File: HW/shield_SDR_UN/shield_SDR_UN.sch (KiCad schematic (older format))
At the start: 1 part

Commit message: Subsystems sheets created
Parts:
- removed U?: XC6SLX9-TQG144, symbol FPGA_Xilinx_Spartan6:XC6SLX9-TQG144
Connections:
- wire segments 2 -> 0
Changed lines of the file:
@@
 $Descr A3 16535 11693
 encoding utf-8
-Sheet 1 1
+Sheet 1 5
 Title ""
 Date ""
@@
 Comment4 ""
 $EndDescr
-$Comp
-L FPGA_Xilinx_Spartan6:XC6SLX9-TQG144 U?
-U 1 1 5CC13A59
-P 4200 3250
-F 0 "U?" H 4200 1475 50  0000 C CNN
-F 1 "XC6SLX9-TQG144" H 4200 1384 50  0000 C CNN
-F 2 "" H 4200 3250 50  0001 C CNN
-F 3 "" H 4200 3250 50  0000 C CNN
-	1    4200 3250
-	1    0    0    -1
-$EndComp
-Wire Wire Line
-	2600 1550 2700 1550
-Wire Wire Line
-	2700 1550 2800 1550
-Connection ~ 2700 1550
+$Sheet
+S 3900 2800 1100 300
+U 5CC081D2
+F0 "rf_front_end" 50
+F1 "rf_front_end.sch" 50
+$EndSheet
+$Sheet
+S 3900 3350 1100 300
+U 5CC08265
+F0 "FPGA" 50
+F1 "FPGA.sch" 50
+$EndSheet
+$Sheet
+S 3900 3900 1100 300
+U 5CC082AD
+F0 "proc" 50
+F1 "proc.sch" 50
+$EndSheet
+$Sheet
+S 3900 4500 1100 300
+U 5CC08321
+F0 "power" 50
+F1 "power.sch" 50
+$EndSheet
 $EndSCHEMATC

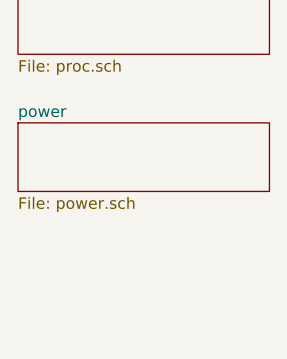
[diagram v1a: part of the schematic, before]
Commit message: Onion 2 routed
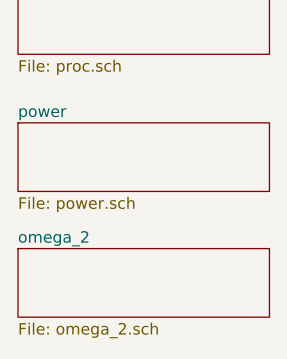
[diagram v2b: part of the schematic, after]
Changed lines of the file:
@@
 $Descr A3 16535 11693
 encoding utf-8
-Sheet 1 5
+Sheet 1 6
 Title ""
 Date ""
@@
 F1 "power.sch" 50
 $EndSheet
+$Sheet
+S 3900 5050 1100 300
+U 5CFB52DC
+F0 "omega_2" 50
+F1 "omega_2.sch" 50
+$EndSheet
 $EndSCHEMATC

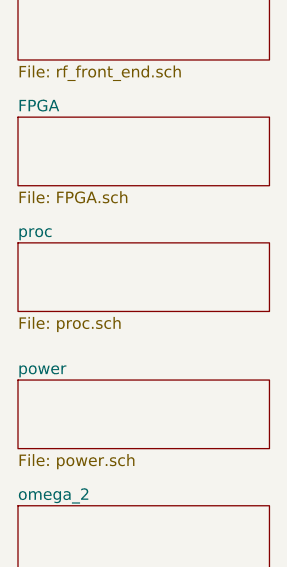
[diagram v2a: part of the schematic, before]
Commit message: se agrego el chip multirelojes
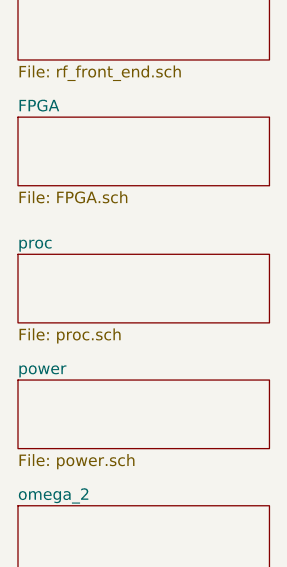
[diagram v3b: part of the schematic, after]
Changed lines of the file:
@@
 $EndSheet
 $Sheet
-S 3900 3900 1100 300
+S 3900 3950 1100 300
 U 5CC082AD
 F0 "proc" 50

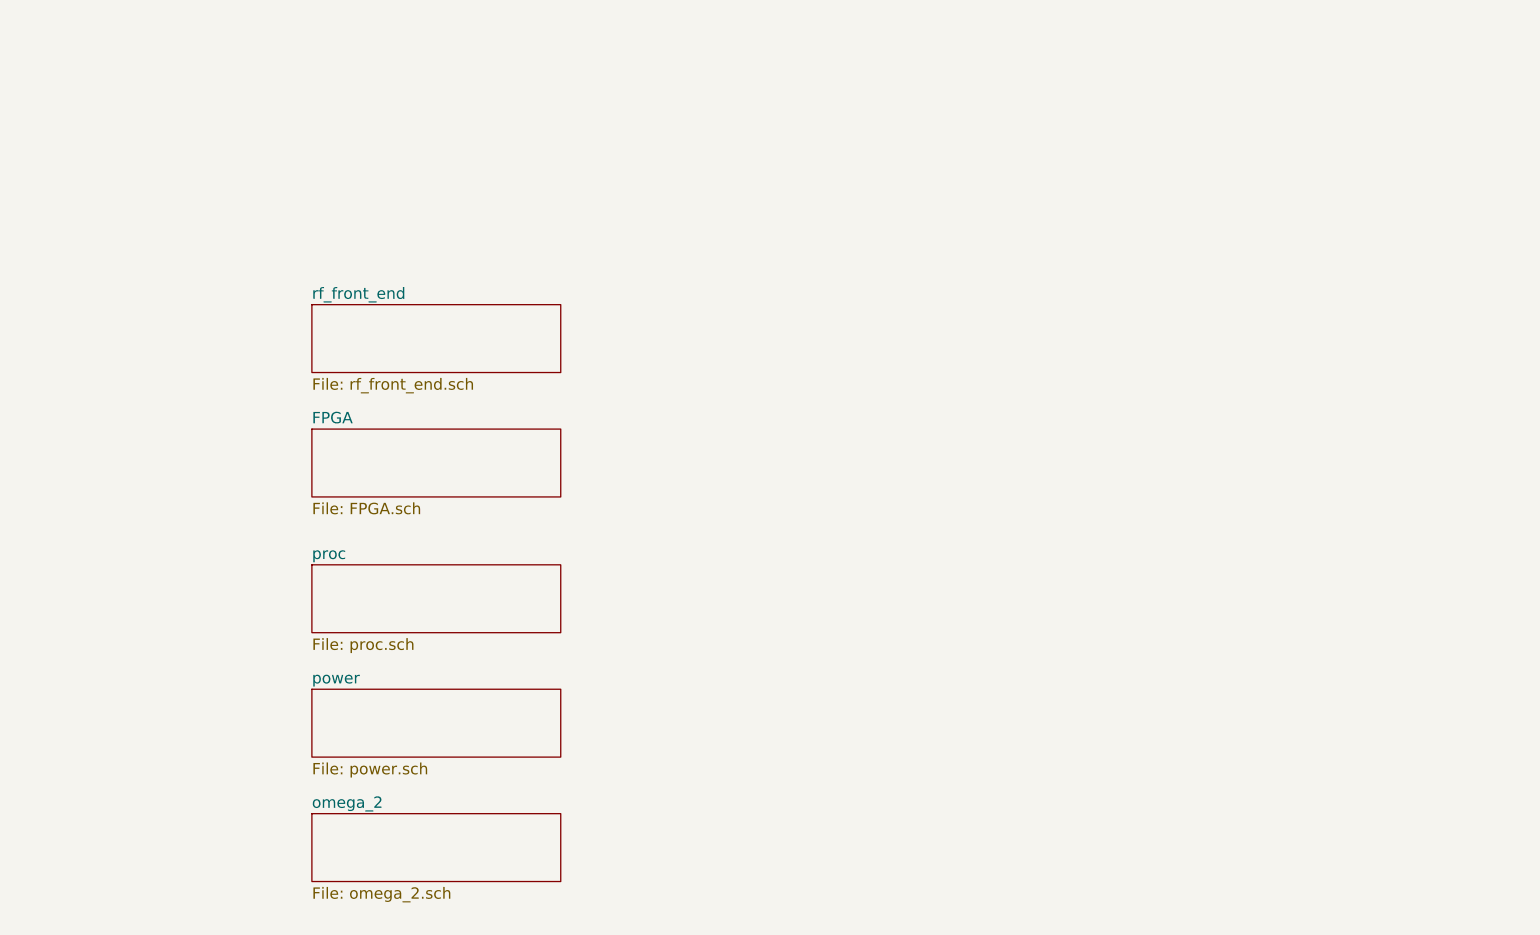
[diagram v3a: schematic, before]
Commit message: JTAG routed
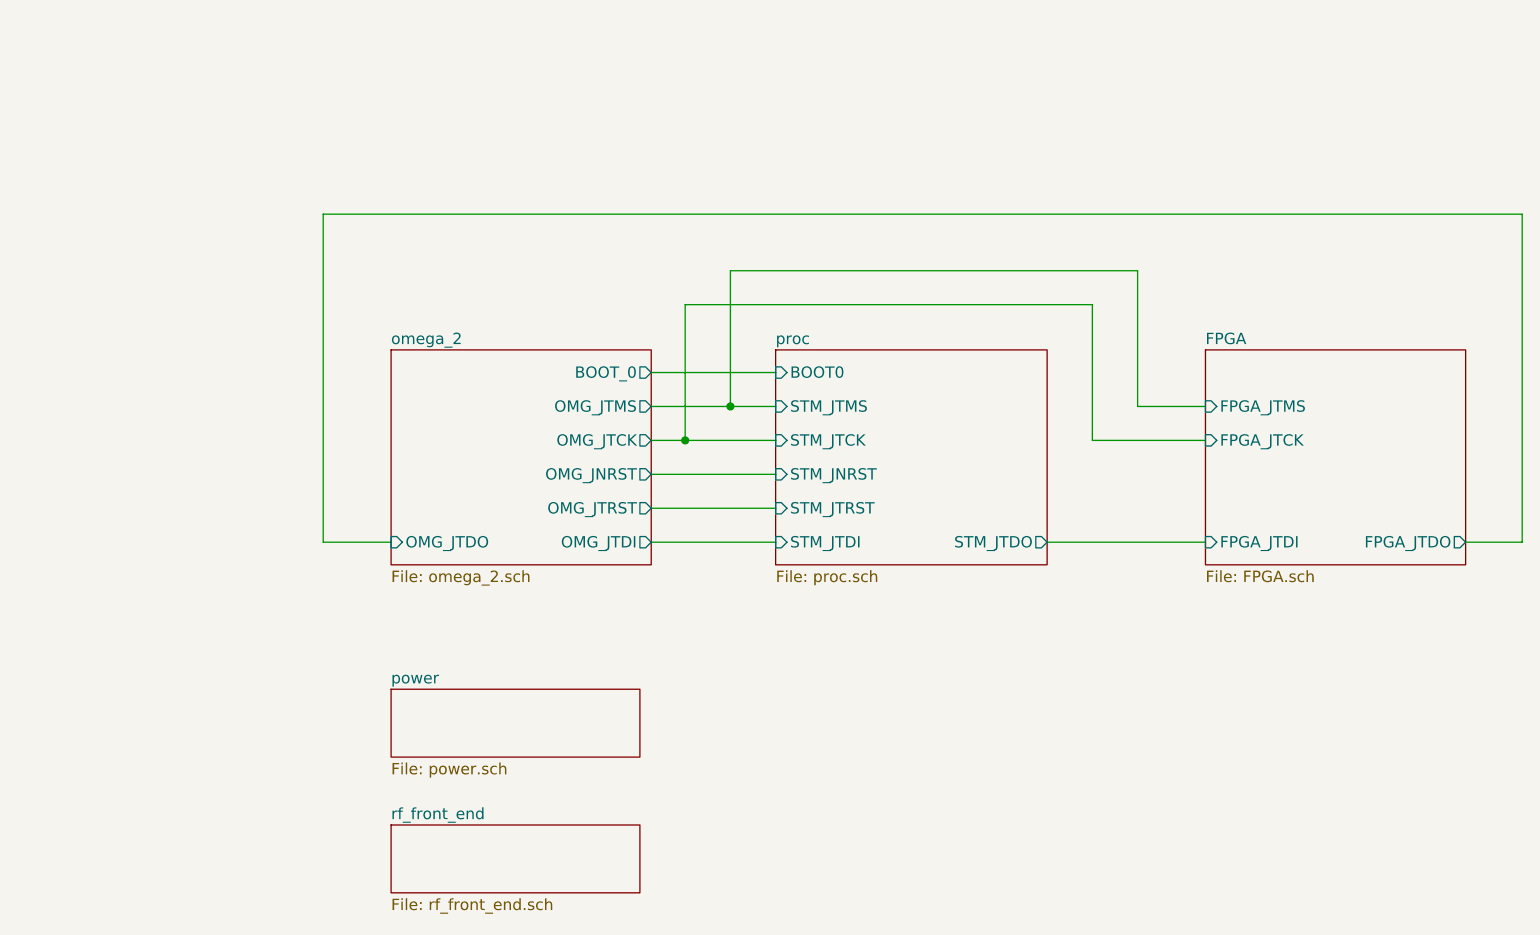
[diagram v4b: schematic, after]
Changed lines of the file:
@@
 $EndDescr
 $Sheet
-S 3900 2800 1100 300
+S 4250 5100 1100 300
 U 5CC081D2
 F0 "rf_front_end" 50
@@
 $EndSheet
 $Sheet
-S 3900 3350 1100 300
+S 7850 3000 1150 950
 U 5CC08265
 F0 "FPGA" 50
 F1 "FPGA.sch" 50
+F2 "FPGA_JTCK" I L 7850 3400 50
+F3 "FPGA_JTDI" I L 7850 3850 50
+F4 "FPGA_JTMS" I L 7850 3250 50
+F5 "FPGA_JTDO" O R 9000 3850 50
 $EndSheet
 $Sheet
-S 3900 3950 1100 300
+S 5950 3000 1200 950
 U 5CC082AD
 F0 "proc" 50
 F1 "proc.sch" 50
+F2 "BOOT0" I L 5950 3100 50
+F3 "STM_JTDO" O R 7150 3850 50
+F4 "STM_JTRST" I L 5950 3700 50
+F5 "STM_JTDI" I L 5950 3850 50
+F6 "STM_JTCK" I L 5950 3400 50
+F7 "STM_JTMS" I L 5950 3250 50
+F8 "STM_JNRST" I L 5950 3550 50
 $EndSheet
 $Sheet
-S 3900 4500 1100 300
+S 4250 4500 1100 300
 U 5CC08321
 F0 "power" 50
@@
 $EndSheet
 $Sheet
-S 3900 5050 1100 300
+S 4250 3000 1150 950
 U 5CFB52DC
 F0 "omega_2" 50
 F1 "omega_2.sch" 50
+F2 "BOOT_0" O R 5400 3100 50
+F3 "OMG_JTMS" O R 5400 3250 50
+F4 "OMG_JTCK" O R 5400 3400 50
+F5 "OMG_JTDI" O R 5400 3850 50
+F6 "OMG_JTRST" O R 5400 3700 50
+F7 "OMG_JNRST" O R 5400 3550 50
+F8 "OMG_JTDO" I L 4250 3850 50
 $EndSheet
+Wire Wire Line
+	5400 3100 5950 3100
+Wire Wire Line
+	5400 3250 5750 3250
+Wire Wire Line
+	5950 3400 5550 3400
+Wire Wire Line
+	5400 3550 5950 3550
+Wire Wire Line
+	5950 3700 5400 3700
+Wire Wire Line
+	5400 3850 5950 3850
+Wire Wire Line
+	7150 3850 7850 3850
+Wire Wire Line
+	7850 3400 7350 3400
+Wire Wire Line
+	7350 3400 7350 2800
+Wire Wire Line
+	7350 2800 5550 2800
+Wire Wire Line
+	5550 2800 5550 3400
+Connection ~ 5550 3400
+Wire Wire Line
+	5550 3400 5400 3400
+Wire Wire Line
+	5750 3250 5750 2650
+Wire Wire Line
+	5750 2650 7550 2650
+Wire Wire Line
+	7550 2650 7550 3250
+Wire Wire Line
+	7550 3250 7850 3250
+Connection ~ 5750 3250
+Wire Wire Line
+	5750 3250 5950 3250
+Wire Wire Line
+	9000 3850 9250 3850
+Wire Wire Line
+	9250 3850 9250 2400
+Wire Wire Line
+	9250 2400 3950 2400
+Wire Wire Line
+	3950 2400 3950 3850
+Wire Wire Line
+	3950 3850 4250 3850
 $EndSCHEMATC

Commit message: i2c_complete
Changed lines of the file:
@@
 	9000 3850 9250 3850
 Wire Wire Line
-	9250 3850 9250 2400
+	3950 3850 4250 3850
 Wire Wire Line
-	9250 2400 3950 2400
+	3950 3850 3950 4250
 Wire Wire Line
-	3950 2400 3950 3850
+	3950 4250 9250 4250
 Wire Wire Line
-	3950 3850 4250 3850
+	9250 4250 9250 3850
 $EndSCHEMATC

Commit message: Schematic finished
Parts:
- added H1, H2, H3, H4: MountingHole, MountingHole:MountingHole_2.7mm_M2.5_ISO14580_Pad, symbol Mechanical:MountingHole
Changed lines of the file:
@@
 Wire Wire Line
 	9250 4250 9250 3850
+$Comp
+L Mechanical:MountingHole H1
+U 1 1 5CF719B7
+P 6125 4550
+F 0 "H1" H 6225 4596 50  0000 L CNN
+F 1 "MountingHole" H 6225 4505 50  0000 L CNN
+F 2 "MountingHole:MountingHole_2.7mm_M2.5_ISO14580_Pad" H 6125 4550 50  0001 C CNN
+F 3 "~" H 6125 4550 50  0001 C CNN
+	1    6125 4550
+	1    0    0    -1
+$EndComp
+$Comp
+L Mechanical:MountingHole H2
+U 1 1 5CF73518
+P 6125 4775
+F 0 "H2" H 6225 4821 50  0000 L CNN
+F 1 "MountingHole" H 6225 4730 50  0000 L CNN
+F 2 "MountingHole:MountingHole_2.7mm_M2.5_ISO14580_Pad" H 6125 4775 50  0001 C CNN
+F 3 "~" H 6125 4775 50  0001 C CNN
+	1    6125 4775
+	1    0    0    -1
+$EndComp
+$Comp
+L Mechanical:MountingHole H3
+U 1 1 5CF735B5
+P 6125 5000
+F 0 "H3" H 6225 5046 50  0000 L CNN
+F 1 "MountingHole" H 6225 4955 50  0000 L CNN
+F 2 "MountingHole:MountingHole_2.7mm_M2.5_ISO14580_Pad" H 6125 5000 50  0001 C CNN
+F 3 "~" H 6125 5000 50  0001 C CNN
+	1    6125 5000
+	1    0    0    -1
+$EndComp
+$Comp
+L Mechanical:MountingHole H4
+U 1 1 5CF7376A
+P 6125 5225
+F 0 "H4" H 6225 5271 50  0000 L CNN
+F 1 "MountingHole" H 6225 5180 50  0000 L CNN
+F 2 "MountingHole:MountingHole_2.7mm_M2.5_ISO14580_Pad" H 6125 5225 50  0001 C CNN
+F 3 "~" H 6125 5225 50  0001 C CNN
+	1    6125 5225
+	1    0    0    -1
+$EndComp
 $EndSCHEMATC
